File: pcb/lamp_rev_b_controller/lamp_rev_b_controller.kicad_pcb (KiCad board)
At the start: 4 copper layers, 118 x 88 mm, 155 parts, among them J1 TYPE-C 3.1 MT 16P, J10 2-pin NTC header, J11 2-pin NTC header, J12 DB128H-5.08-2P-BK-S, J13 DB128H-5.08-2P-BK-S, J15 DB128H-5.08-2P-BK-S, J16 LED NTC/ID header, J17 External camera sync header, J18 SPI/FIFO camera module header, J19 Lid/cartridge/cutoff interloc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, J2 DB128H-5.08-2P-BK-S, J20 Fan PWM/tach header, J21 2x3 UART/programming header, J22 I2C expansion header, J23 Analog optical diagnostic hea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, J24 DB128H-5.08-2P high-current h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, J4 2-pin NTC header, J5 2-pin NTC header, J6 2-pin NTC header, J7 2-pin NTC header, J8 2-pin NTC header, J9 2-pin NTC header, Q1 IRLB3813PBF TO-220 12V protot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, Q2 IRLB3813PBF TO-220 12V protot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, U1 ESP32-S3-WROOM-1-N16, U10 INA180A1IDBVR gain 20 LED cur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, U2 USBLC6-2SC6, U3 Diodes AP63203WU-7 fixed 3.3V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, U4 ADS1115IDGSR, U5 CD74HC4051M, U6 TC4427ACOA/TC4427EPA, U7 CUI/Bel P7805-2000-S 5V 2A 8-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, U8 Mean Well LDD-700H 700mA CC b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, U9 SN74LVC1G08DBVR LED_EXC_PWM A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

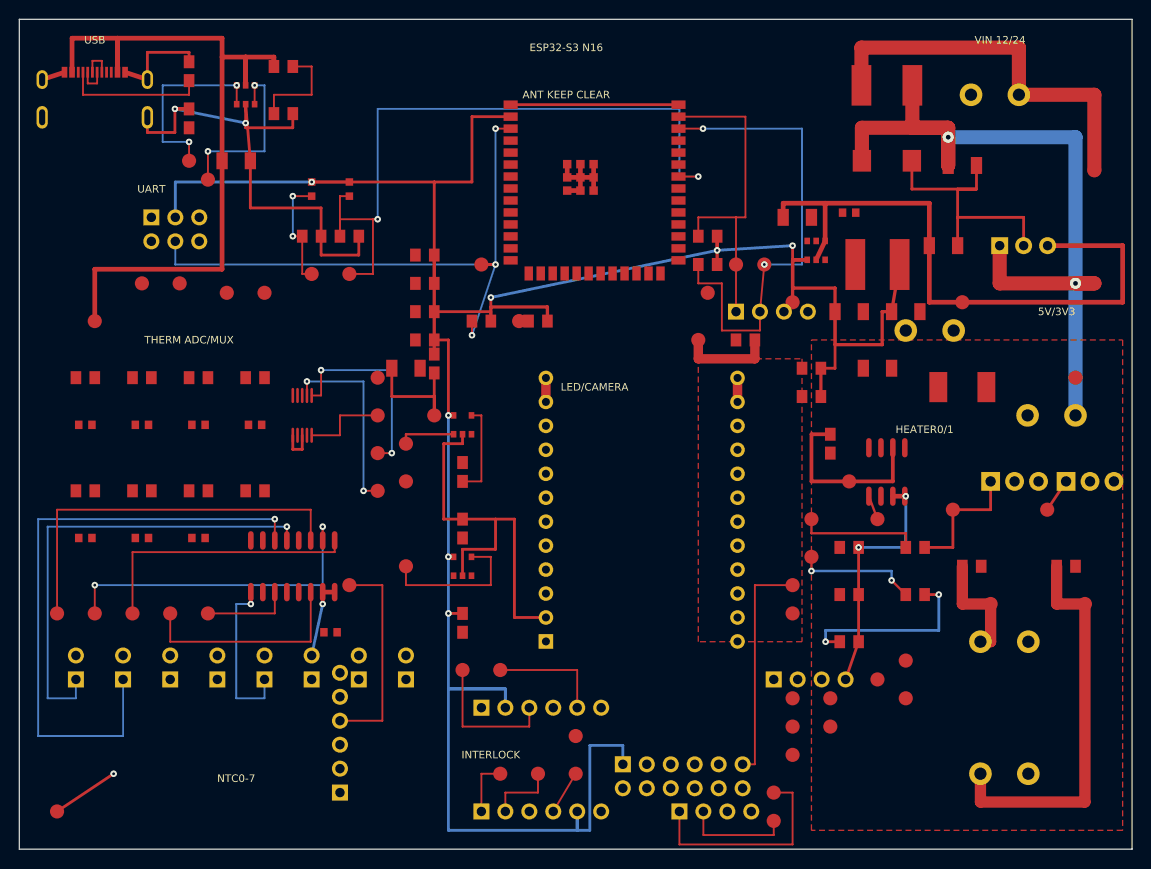
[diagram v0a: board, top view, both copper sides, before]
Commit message: Reduce Rev B controller routing to 100 unconnected
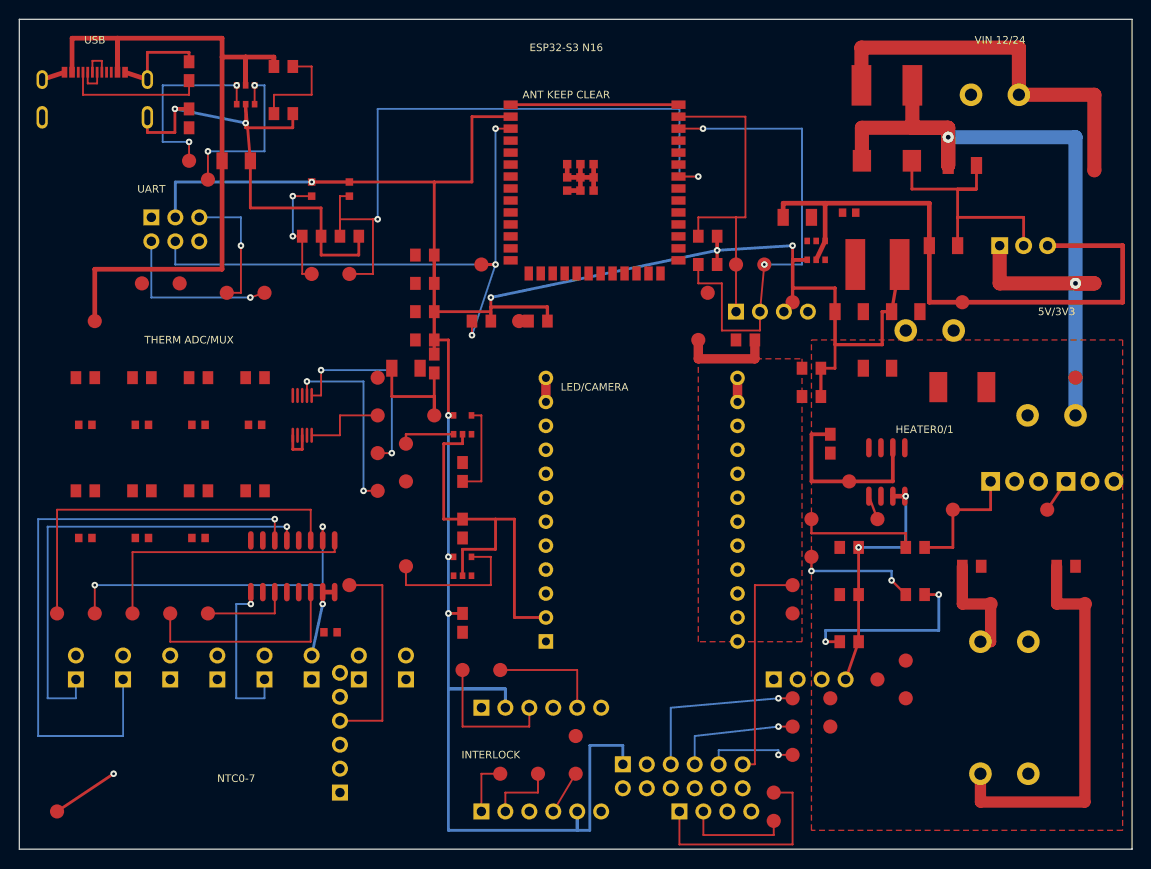
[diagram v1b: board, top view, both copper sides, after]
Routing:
- net SPI_SCLK: track 0.00 -> 19.0 mm, vias 0 -> 1
- net UART0_RXD: track 0.00 -> 18.0 mm, vias 0 -> 1
- net UART0_TXD: track 0.00 -> 13.9 mm, vias 0 -> 1
- net SPI_MOSI: track 0.00 -> 13.4 mm, vias 0 -> 1
- net SPI_MISO: track 0.00 -> 9.84 mm, vias 0 -> 1
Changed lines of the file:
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@@
     (net 73)
+  )
+  (via
+    (at 80.500 78)
+    (size 0.700)
+    (drill 0.300)
+    (layers "F.Cu" "B.Cu")
+    (net 26)
+  )
+  (via
+    (at 80.500 75)
+    (size 0.700)
+    (drill 0.300)
+    (layers "F.Cu" "B.Cu")
+    (net 25)
+  )
+  (via
+    (at 80.500 72)
+    (size 0.700)
+    (drill 0.300)
+    (layers "F.Cu" "B.Cu")
+    (net 24)
+  )
+  (via
+    (at 23.500 24)
+    (size 0.700)
+    (drill 0.300)
+    (layers "F.Cu" "B.Cu")
+    (net 20)
+  )
+  (via
+    (at 24.500 29.500)
+    (size 0.700)
+    (drill 0.300)
+    (layers "F.Cu" "B.Cu")
+    (net 21)
   )
   (segment
@@
     (net 73)
   )
+  (segment
+    (start 74.160 79)
+    (end 74.160 77.500)
+    (width 0.200)
+    (layer "B.Cu")
+    (net 26)
+  )
+  (segment
+    (start 74.160 77.500)
+    (end 80.500 77.500)
+    (width 0.200)
+    (layer "B.Cu")
+    (net 26)
+  )
+  (segment
+    (start 80.500 77.500)
+    (end 80.500 78)
+    (width 0.200)
+    (layer "B.Cu")
+    (net 26)
+  )
+  (segment
+    (start 80.500 78)
+    (end 82 78)
+    (width 0.200)
+    (layer "F.Cu")
+    (net 26)
+  )
+  (segment
+    (start 71.620 79)
+    (end 71.620 76)
+    (width 0.200)
+    (layer "B.Cu")
+    (net 25)
+  )
+  (segment
+    (start 71.620 76)
+    (end 80.500 75)
+    (width 0.200)
+    (layer "B.Cu")
+    (net 25)
+  )
+  (segment
+    (start 80.500 75)
+    (end 82 75)
+    (width 0.200)
+    (layer "F.Cu")
+    (net 25)
+  )
+  (segment
+    (start 69.080 79)
+    (end 69.080 73)
+    (width 0.200)
+    (layer "B.Cu")
+    (net 24)
+  )
+  (segment
+    (start 69.080 73)
+    (end 80.500 72)
+    (width 0.200)
+    (layer "B.Cu")
+    (net 24)
+  )
+  (segment
+    (start 80.500 72)
+    (end 82 72)
+    (width 0.200)
+    (layer "F.Cu")
+    (net 24)
+  )
+  (segment
+    (start 19.080 21)
+    (end 23.500 21)
+    (width 0.200)
+    (layer "B.Cu")
+    (net 20)
+  )
+  (segment
+    (start 23.500 21)
+    (end 23.500 24)
+    (width 0.200)
+    (layer "B.Cu")
+    (net 20)
+  )
+  (segment
+    (start 23.500 24)
+    (end 23.500 29)
+    (width 0.200)
+    (layer "F.Cu")
+    (net 20)
+  )
+  (segment
+    (start 23.500 29)
+    (end 22 29)
+    (width 0.200)
+    (layer "F.Cu")
+    (net 20)
+  )
+  (segment
+    (start 14 23.540)
+    (end 14 29.500)
+    (width 0.200)
+    (layer "B.Cu")
+    (net 21)
+  )
+  (segment
+    (start 14 29.500)
+    (end 24.500 29.500)
+    (width 0.200)
+    (layer "B.Cu")
+    (net 21)
+  )
+  (segment
+    (start 24.500 29.500)
+    (end 26 29)
+    (width 0.200)
+    (layer "F.Cu")
+    (net 21)
+  )
   (zone

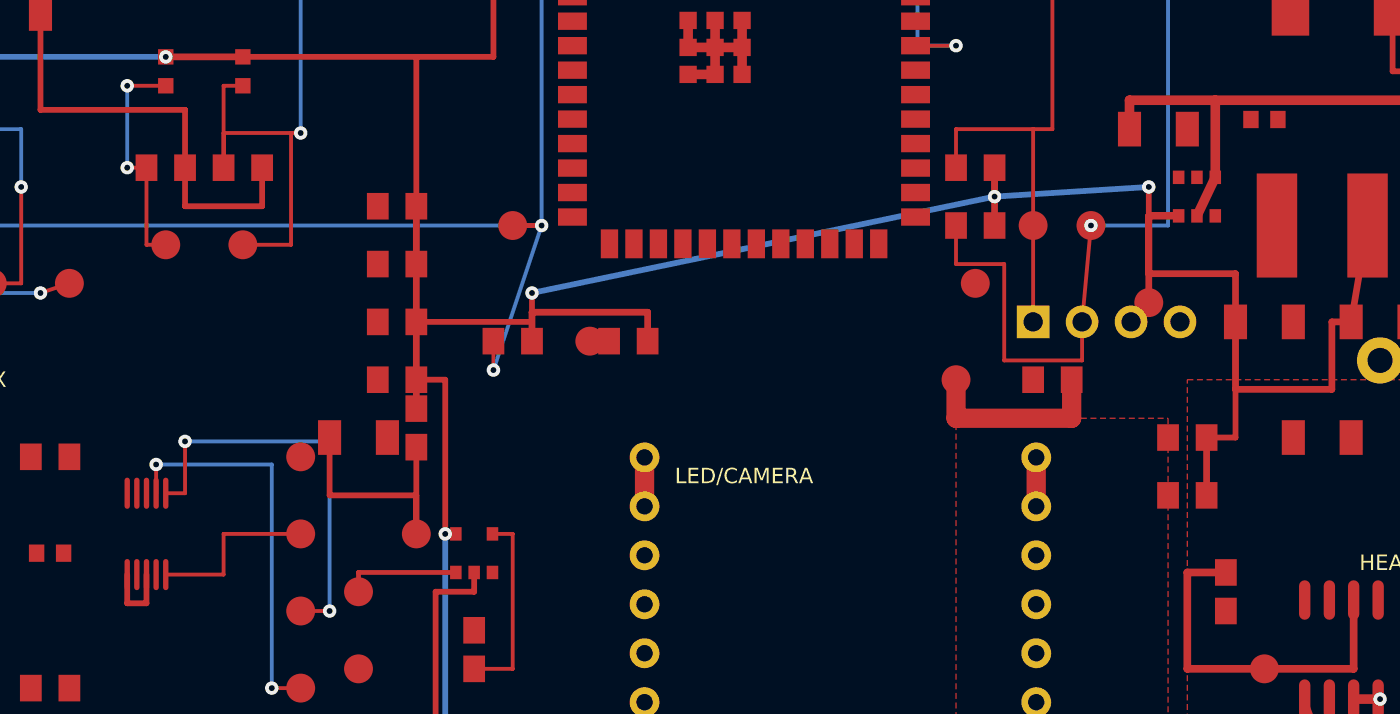
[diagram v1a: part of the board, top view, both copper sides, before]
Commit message: Reduce Rev B controller routing to 94 unconnected
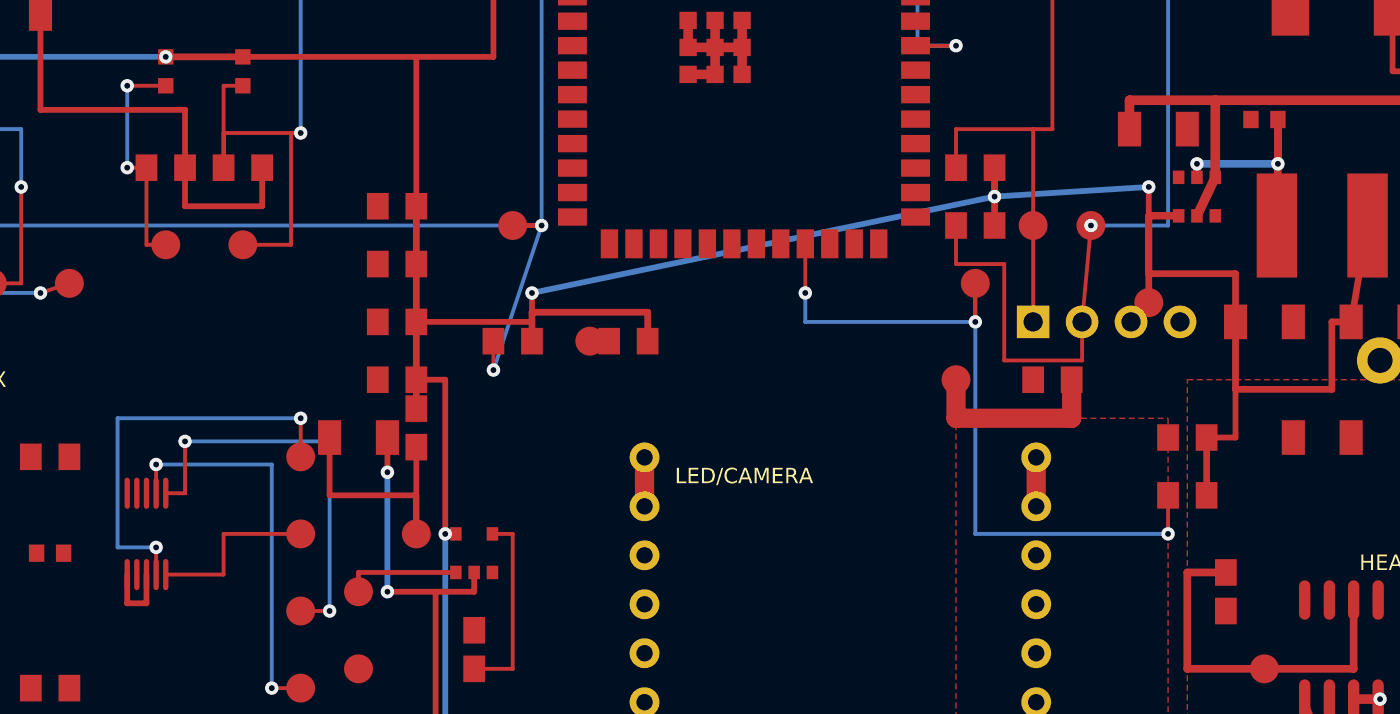
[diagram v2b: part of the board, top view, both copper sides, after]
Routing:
- net SD_CS_N: track 0.00 -> 39.9 mm, vias 0 -> 3
- net ADS_AIN0: track 0.00 -> 21.6 mm, vias 0 -> 2
- net 3V3_SW: track 0.00 -> 12.7 mm, vias 0 -> 2
- net GND: track 206.0 -> 216.5 mm, vias 6 -> 8
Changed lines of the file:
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@@
     (net 21)
+  )
+  (via
+    (at 42.500 38.800)
+    (size 0.700)
+    (drill 0.300)
+    (layers "F.Cu" "B.Cu")
+    (net 1)
+  )
+  (via
+    (at 42.500 45)
+    (size 0.700)
+    (drill 0.300)
+    (layers "F.Cu" "B.Cu")
+    (net 1)
+  )
+  (via
+    (at 30.500 42.700)
+    (size 0.700)
+    (drill 0.300)
+    (layers "F.Cu" "B.Cu")
+    (net 45)
+  )
+  (via
+    (at 38 36)
+    (size 0.700)
+    (drill 0.300)
+    (layers "F.Cu" "B.Cu")
+    (net 45)
+  )
+  (via
+    (at 83 42)
+    (size 0.700)
+    (drill 0.300)
+    (layers "F.Cu" "B.Cu")
+    (net 31)
+  )
+  (via
+    (at 73 31)
+    (size 0.700)
+    (drill 0.300)
+    (layers "F.Cu" "B.Cu")
+    (net 31)
+  )
+  (via
+    (at 64.180 29.500)
+    (size 0.700)
+    (drill 0.300)
+    (layers "F.Cu" "B.Cu")
+    (net 31)
+  )
+  (via
+    (at 84.500 22.800)
+    (size 0.700)
+    (drill 0.300)
+    (layers "F.Cu" "B.Cu")
+    (net 10)
+  )
+  (via
+    (at 88.700 22.800)
+    (size 0.700)
+    (drill 0.300)
+    (layers "F.Cu" "B.Cu")
+    (net 10)
   )
   (segment
@@
   )
   (segment
+    (start 83 40)
+    (end 83 42)
+    (width 0.200)
+    (layer "F.Cu")
+    (net 31)
+  )
+  (segment
+    (start 83 42)
+    (end 73 42)
+    (width 0.200)
+    (layer "B.Cu")
+    (net 31)
+  )
+  (segment
+    (start 73 42)
+    (end 73 31)
+    (width 0.200)
+    (layer "B.Cu")
+    (net 31)
+  )
+  (segment
+    (start 73 31)
+    (end 73 29)
+    (width 0.200)
+    (layer "F.Cu")
+    (net 31)
+  )
+  (segment
+    (start 73 29)
+    (end 73 31)
+    (width 0.200)
+    (layer "F.Cu")
+    (net 31)
+  )
+  (segment
+    (start 73 31)
+    (end 64.180 31)
+    (width 0.200)
+    (layer "B.Cu")
+    (net 31)
+  )
+  (segment
+    (start 64.180 31)
+    (end 64.180 29.500)
+    (width 0.200)
+    (layer "B.Cu")
+    (net 31)
+  )
+  (segment
+    (start 64.180 29.500)
+    (end 64.180 26.950)
+    (width 0.200)
+    (layer "F.Cu")
+    (net 31)
+  )
+  (segment
     (start 100 30)
     (end 117 30)
@@
     (layer "F.Cu")
     (net 8)
+  )
+  (segment
+    (start 84.500 23.500)
+    (end 84.500 22.800)
+    (width 0.400)
+    (layer "F.Cu")
+    (net 10)
+  )
+  (segment
+    (start 84.500 22.800)
+    (end 88.700 22.800)
+    (width 0.400)
+    (layer "B.Cu")
+    (net 10)
+  )
+  (segment
+    (start 88.700 22.800)
+    (end 88.700 20.500)
+    (width 0.400)
+    (layer "F.Cu")
+    (net 10)
+  )
+  (segment
+    (start 88.700 20.500)
+    (end 88.700 22.800)
+    (width 0.400)
+    (layer "F.Cu")
+    (net 10)
+  )
+  (segment
+    (start 88.700 22.800)
+    (end 88.650 26)
+    (width 0.400)
+    (layer "F.Cu")
+    (net 10)
   )
   (segment
@@
   )
   (segment
+    (start 30.500 44.110)
+    (end 30.500 42.700)
+    (width 0.200)
+    (layer "F.Cu")
+    (net 45)
+  )
+  (segment
+    (start 30.500 42.700)
+    (end 28.500 42.700)
+    (width 0.200)
+    (layer "B.Cu")
+    (net 45)
+  )
+  (segment
+    (start 28.500 42.700)
+    (end 28.500 36)
+    (width 0.200)
+    (layer "B.Cu")
+    (net 45)
+  )
+  (segment
+    (start 28.500 36)
+    (end 38 36)
+    (width 0.200)
+    (layer "B.Cu")
+    (net 45)
+  )
+  (segment
+    (start 38 36)
+    (end 38 38)
+    (width 0.200)
+    (layer "F.Cu")
+    (net 45)
+  )
+  (segment
     (start 30.500 39.890)
     (end 30.500 38.400)
@@
     (width 0.300)
     (layer "F.Cu")
+    (net 1)
+  )
+  (segment
+    (start 42.500 37)
+    (end 42.500 38.800)
+    (width 0.300)
+    (layer "F.Cu")
+    (net 1)
+  )
+  (segment
+    (start 42.500 38.800)
+    (end 42.500 45)
+    (width 0.300)
+    (layer "B.Cu")
+    (net 1)
+  )
+  (segment
+    (start 42.500 45)
+    (end 45 45)
+    (width 0.300)
+    (layer "F.Cu")

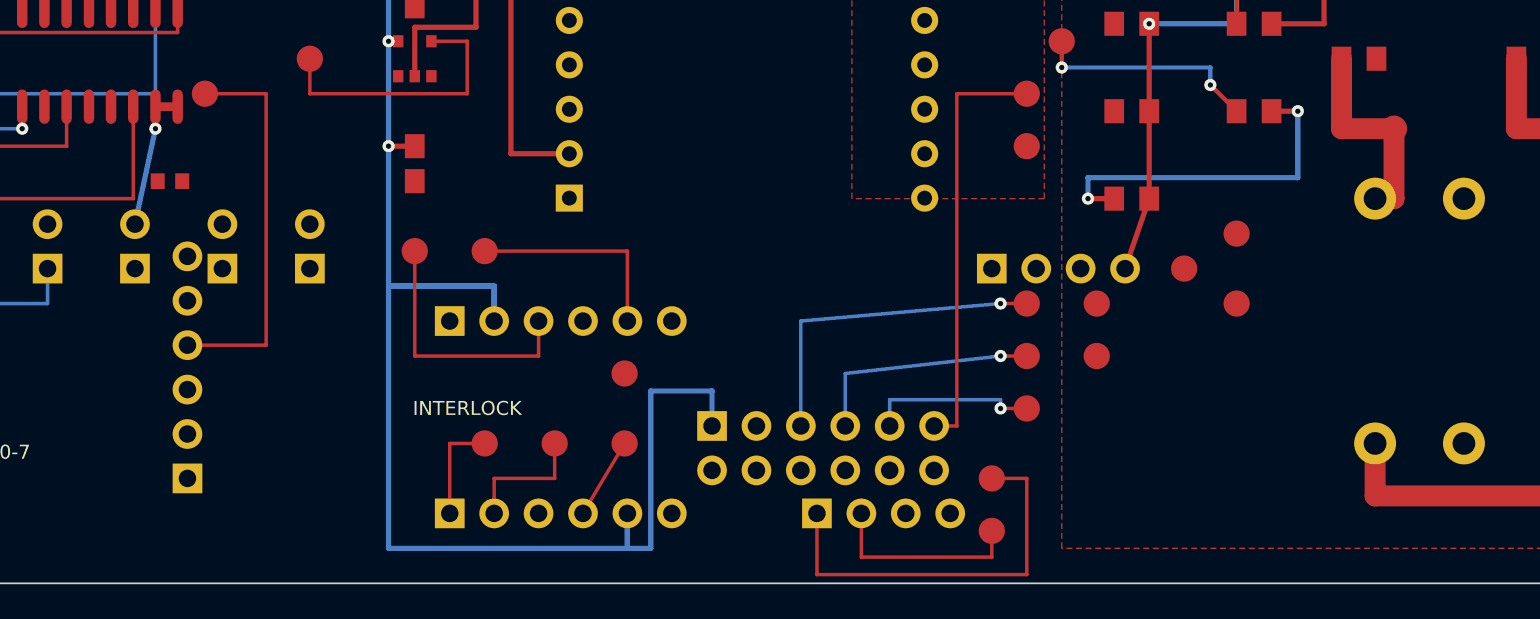
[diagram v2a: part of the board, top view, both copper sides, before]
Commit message: Reduce Rev B controller routing to 91 unconnected
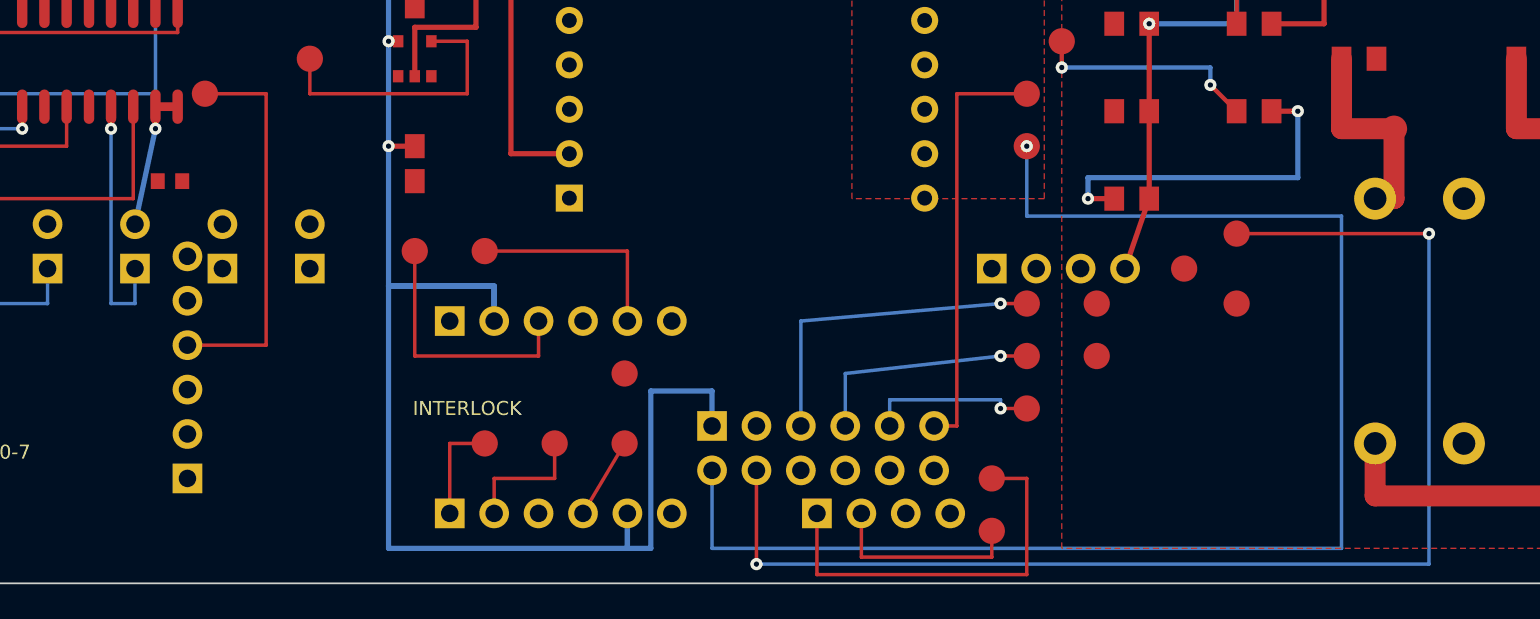
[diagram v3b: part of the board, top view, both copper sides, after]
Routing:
- net CAM_FRAME_INT: track 0.00 -> 81.5 mm, vias 0 -> 1
- net CAM_RESET_N: track 0.00 -> 73.7 mm, vias 0 -> 2
- net THERM_CH_5: track 0.00 -> 14.6 mm, vias 0 -> 1
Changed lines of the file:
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@@
     (net 10)
+  )
+  (via
+    (at 82 63)
+    (size 0.700)
+    (drill 0.300)
+    (layers "F.Cu" "B.Cu")
+    (net 28)
+  )
+  (via
+    (at 105 68)
+    (size 0.700)
+    (drill 0.300)
+    (layers "F.Cu" "B.Cu")
+    (net 29)
+  )
+  (via
+    (at 66.540 86.900)
+    (size 0.700)
+    (drill 0.300)
+    (layers "F.Cu" "B.Cu")
+    (net 29)
+  )
+  (via
+    (at 29.630 62)
+    (size 0.700)
+    (drill 0.300)
+    (layers "F.Cu" "B.Cu")
+    (net 77)
   )
   (segment
@@
     (net 21)
   )
+  (segment
+    (start 64 81.540)
+    (end 64 86)
+    (width 0.200)
+    (layer "B.Cu")
+    (net 28)
+  )
+  (segment
+    (start 64 86)
+    (end 100 86)
+    (width 0.200)
+    (layer "B.Cu")
+    (net 28)
+  )
+  (segment
+    (start 100 86)
+    (end 100 67)
+    (width 0.200)
+    (layer "B.Cu")
+    (net 28)
+  )
+  (segment
+    (start 100 67)
+    (end 82 67)
+    (width 0.200)
+    (layer "B.Cu")
+    (net 28)
+  )
+  (segment
+    (start 82 67)
+    (end 82 63)
+    (width 0.200)
+    (layer "B.Cu")
+    (net 28)
+  )
+  (segment
+    (start 66.540 81.540)
+    (end 66.540 86.900)
+    (width 0.200)
+    (layer "F.Cu")
+    (net 29)
+  )
+  (segment
+    (start 66.540 86.900)
+    (end 105 86.900)
+    (width 0.200)
+    (layer "B.Cu")
+    (net 29)
+  )
+  (segment
+    (start 105 86.900)
+    (end 105 68)
+    (width 0.200)
+    (layer "B.Cu")
+    (net 29)
+  )
+  (segment
+    (start 105 68)
+    (end 94 68)
+    (width 0.200)
+    (layer "F.Cu")
+    (net 29)
+  )
+  (segment
+    (start 29.630 60.740)
+    (end 29.630 62)
+    (width 0.200)
+    (layer "F.Cu")
+    (net 77)
+  )
+  (segment
+    (start 29.630 62)
+    (end 29.630 72)
+    (width 0.200)
+    (layer "B.Cu")
+    (net 77)
+  )
+  (segment
+    (start 29.630 72)
+    (end 31 72)
+    (width 0.200)
+    (layer "B.Cu")
+    (net 77)
+  )
+  (segment
+    (start 31 72)
+    (end 31 70)
+    (width 0.200)
+    (layer "B.Cu")
+    (net 77)
+  )
   (zone
